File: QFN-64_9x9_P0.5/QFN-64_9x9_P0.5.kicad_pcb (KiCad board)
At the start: 2 copper layers, 25.4 x 86.4 mm, 6 parts, among them J101 Conn_01x12, J102 Conn_01x12, J103 Conn_01x12, J104 Conn_01x12, U101 QFN-64

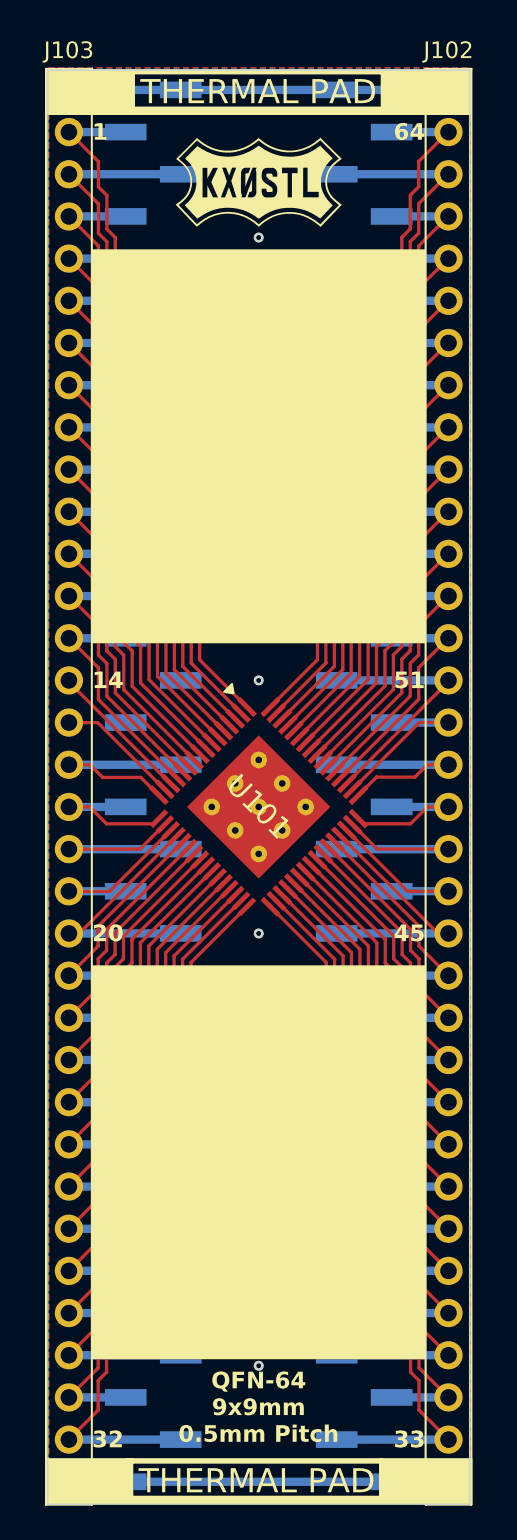
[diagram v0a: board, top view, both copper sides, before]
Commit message: Created SMDIP-16, QFP-48, QFP-32, QFN-80, QFN-68, QFN-64, QFN-60, QFN-56, QFN-48, QFN-36, QFN-28, QFN-20, QFP-32, QFP-48
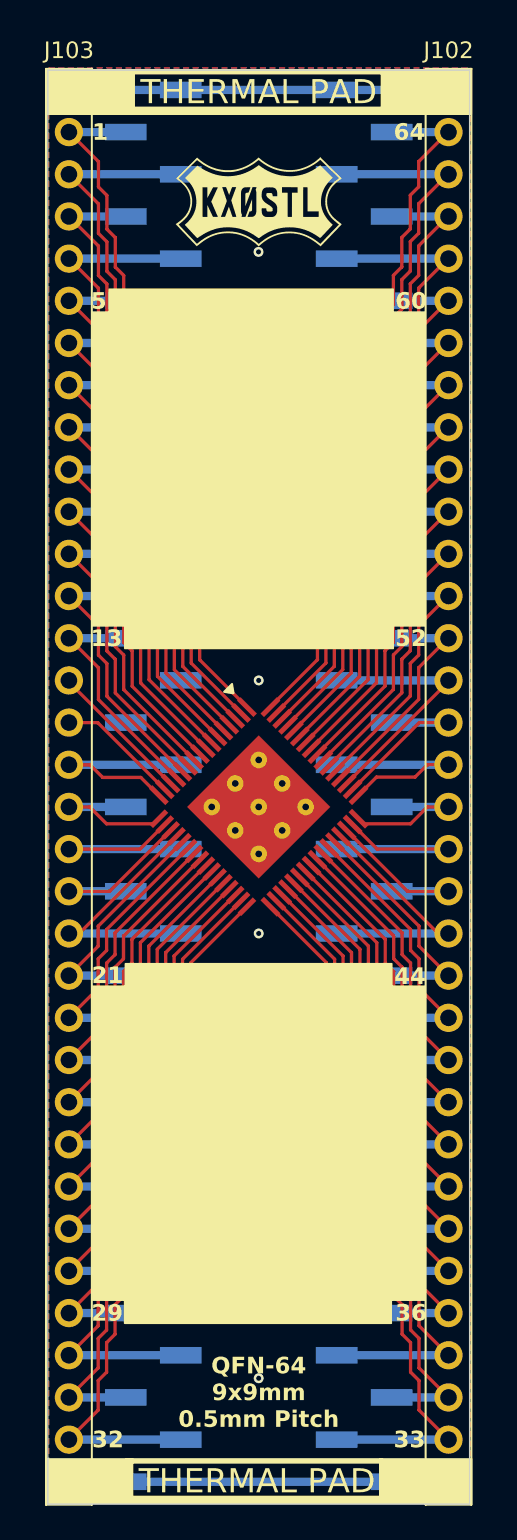
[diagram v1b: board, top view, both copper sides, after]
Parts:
- moved G*** 1.18 mm to (121.4, 86.5)
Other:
- board text added: "13"
- board text added: "21"
- board text added: "29"
- board text added: "36"
- board text added: "44"
- board text added: "5"
- board text added: "52"
- board text added: "60"
- board text removed: "14"
- board text removed: "20"
- board text removed: "45"
- board text removed: "51"
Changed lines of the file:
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@@
 			(at 0 0 135)
 			(layer "F.SilkS")
+			(hide yes)
 			(effects
 				(font
@@
 	(footprint "libraries:Logo_10mm_inv"
 		(layer "F.Cu")
-		(at 121.412 85.316561)
+		(at 121.412 86.492561)
 		(property "Reference" "G***"
 			(at 0 0 0)
@@
 	)
 	(gr_rect
-		(start 111.379 89.408)
-		(end 131.445 113.03)
+		(start 111.379 93.138)
+		(end 131.445 112.03)
+		(stroke
+			(width 0.1)
+			(type solid)
+		)
+		(fill yes)
+		(layer "F.SilkS")
+	)
+	(gr_rect
+		(start 113.339 152.6365)
+		(end 129.395 154.0285)
+		(stroke
+			(width 0.1)
+			(type solid)
+		)
+		(fill yes)
+		(layer "F.SilkS")
+	)
+	(gr_rect
+		(start 113.347 111.228)
+		(end 129.513 113.39)
 		(stroke
 			(width 0.1)
@@
 	)
 	(gr_rect
+		(start 113.387 132.3785)
+		(end 129.423 133.7415)
+		(stroke
+			(width 0.1)
+			(type solid)
+		)
+		(fill yes)
+		(layer "F.SilkS")
+	)
+	(gr_rect
+		(start 112.407 91.76)
+		(end 129.503 93.254)
+		(stroke
+			(width 0.1)
+			(type solid)
+		)
+		(fill yes)
+		(layer "F.SilkS")
+	)
+	(gr_rect
 		(start 113.538 78.549375)
 		(end 128.95575 78.777975)
@@
 	)
 	(gr_rect
-		(start 111.379 132.5245)
-		(end 131.445 156.1465)
+		(start 111.379 133.7345)
+		(end 131.445 152.6365)
 		(stroke
 			(width 0.1)
@@
 		(layer "Edge.Cuts")
 	)
-	(gr_text "14"
-		(at 111.379 115.316 0)
-		(layer "F.SilkS")
+	(gr_text "29"
+		(at 111.33102 153.411951 0)
+		(layer "F.SilkS" knockout)
 		(effects
 			(font
@@
 		)
 	)
+	(gr_text "13"
+		(at 111.29 112.784 0)
+		(layer "F.SilkS" knockout)
+		(effects
+			(font
+				(size 1 1)
+				(thickness 0.2)
+				(bold yes)
+			)
+			(justify left)
+		)
+	)
+	(gr_text "36"
+		(at 131.54 153.406 0)
+		(layer "F.SilkS" knockout)
+		(effects
+			(font
+				(size 1 1)
+				(thickness 0.2)
+				(bold yes)
+			)
+			(justify right)
+		)
+	)
 	(gr_text "64"
 		(at 131.445 82.296 0)
@@
 		)
 	)
-	(gr_text "20"
-		(at 111.379 130.556 0)
-		(layer "F.SilkS")
+	(gr_text "21"
+		(at 111.35 133.08 0)
+		(layer "F.SilkS" knockout)
 		(effects
 			(font
@@
 		)
 	)
-	(gr_text "51"
-		(at 131.445 115.316 0)
-		(layer "F.SilkS")
+	(gr_text "52"
+		(at 131.53 112.78 0)
+		(layer "F.SilkS" knockout)
 		(effects
 			(font
@@
 	)
 	(gr_text "QFN-64\n9x9mm\n0.5mm Pitch"
-		(at 121.412 161.29 0)
+		(at 121.412 160.390269 0)
 		(layer "F.SilkS")
 		(effects
@@
 		)
 	)
-	(gr_text "45"
-		(at 131.445 130.556 0)
-		(layer "F.SilkS")
+	(gr_text "44"
+		(at 131.479208 133.134467 0)
+		(layer "F.SilkS" knockout)
+		(effects
+			(font
+				(size 1 1)
+				(thickness 0.2)
+				(bold yes)
+			)
+			(justify right)
+		)
+	)
+	(gr_text "5"
+		(at 111.3 92.47 0)
+		(layer "F.SilkS" knockout)
+		(effects
+			(font
+				(size 1 1)
+				(thickness 0.2)
+				(bold yes)
+			)
+			(justify left)
+		)
+	)
+	(gr_text "60"
+		(at 131.54 92.47 0)
+		(layer "F.SilkS" knockout)
 		(effects
 			(font
@@
 	)
 	(via
-		(at 121.412 88.646)
+		(at 121.4 89.51)
 		(size 0.6)
 		(drill 0.3)
@@
 	)
 	(via
-		(at 121.412 156.591)
+		(at 121.41 157.34)
 		(size 0.6)
 		(drill 0.3)
